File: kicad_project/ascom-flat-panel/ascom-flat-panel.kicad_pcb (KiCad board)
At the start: 4 copper layers, 55 x 29.5 mm, 14 parts, among them J1 Servo, J2 JST-XH LED, Q1 IRLZ34N, Q2 IRLZ34N, U1 XIAO-SAMD21-DIP

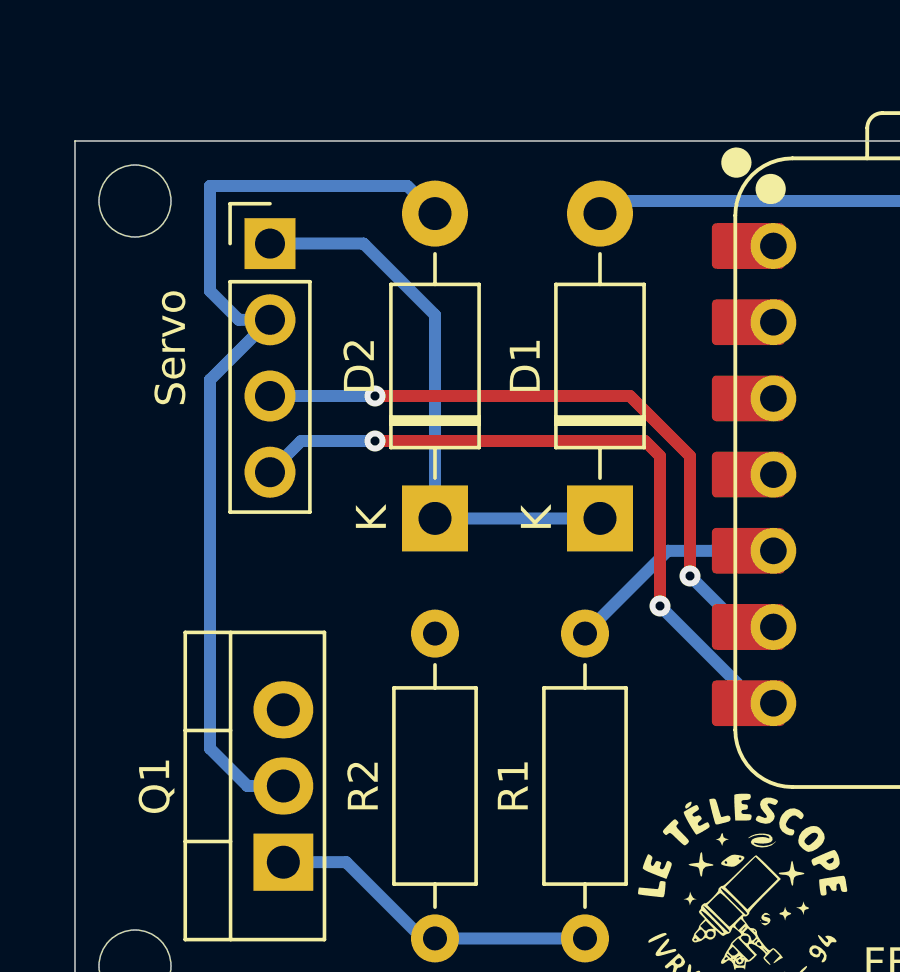
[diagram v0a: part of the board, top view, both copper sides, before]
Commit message: [kicad] - Modif suite aux tests servo : valeur R2 + routage connecteur
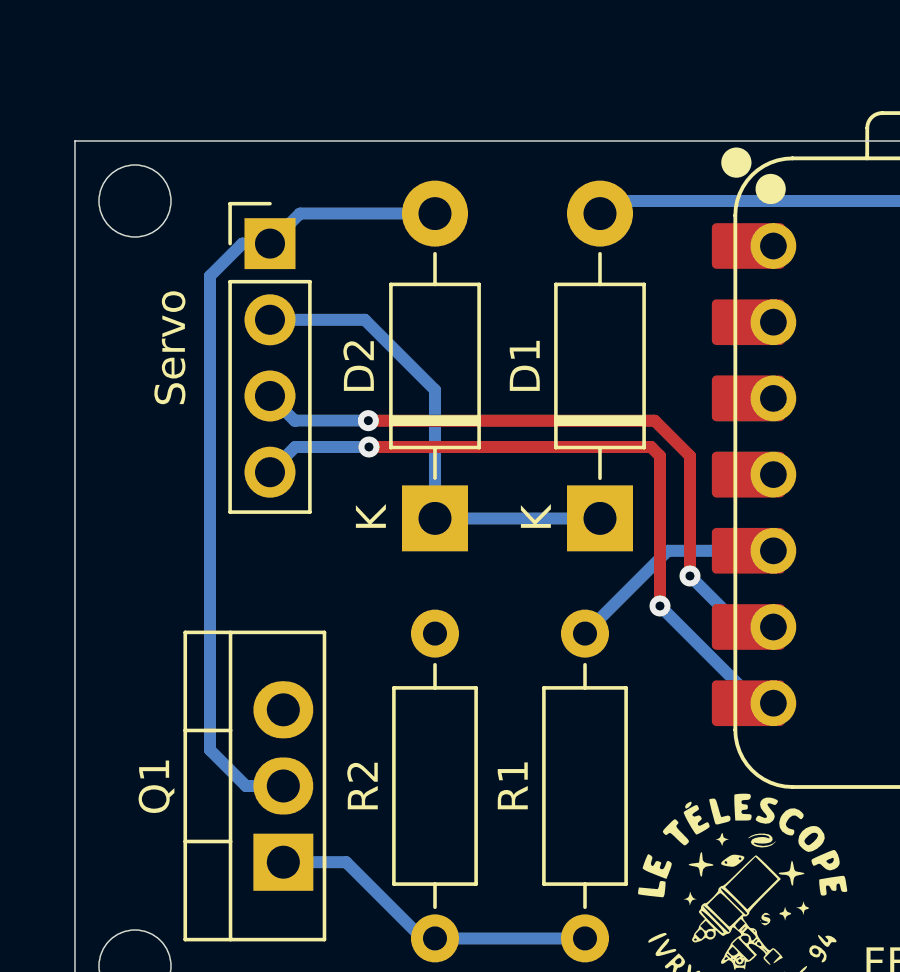
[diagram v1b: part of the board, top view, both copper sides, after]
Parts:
- R2: value 2kΩ -> 2.2kΩ
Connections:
- J1 pad 1: SERVO VCC -> SERVO GND
- J1 pad 2: SERVO GND -> SERVO VCC
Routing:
- net SERVO GND: track 31.9 -> 27.1 mm
- net SERVO VCC: track 18.8 -> 16.2 mm
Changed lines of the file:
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@@
 			)
 		)
-		(property "Value" "2kΩ"
+		(property "Value" "2.2kΩ"
 			(at 5.08 2.37 90)
 			(layer "F.Fab")
@@
 			(layers "*.Cu" "*.Mask")
 			(remove_unused_layers no)
-			(net 3 "SERVO VCC")
+			(net 4 "SERVO GND")
 			(pinfunction "Pin_1")
 			(pintype "passive")
@@
 			(layers "*.Cu" "*.Mask")
 			(remove_unused_layers no)
-			(net 4 "SERVO GND")
+			(net 3 "SERVO VCC")
 			(pinfunction "Pin_2")
 			(pintype "passive")
@@
 	)
 	(segment
-		(start 106.62 72.92)
-		(end 103.5 72.92)
+		(start 114.5 82.08)
+		(end 109 82.08)
 		(width 0.4)
 		(layer "B.Cu")
@@
 	)
 	(segment
-		(start 114.5 82.08)
-		(end 109 82.08)
+		(start 109 82.08)
+		(end 109 77.8)
 		(width 0.4)
 		(layer "B.Cu")
@@
 	)
 	(segment
-		(start 109 75.3)
-		(end 106.62 72.92)
+		(start 109 77.8)
+		(end 106.66 75.46)
 		(width 0.4)
 		(layer "B.Cu")
@@
 	)
 	(segment
-		(start 109 82.08)
-		(end 109 75.3)
+		(start 106.66 75.46)
+		(end 103.5 75.46)
 		(width 0.4)
 		(layer "B.Cu")
@@
 	)
 	(segment
-		(start 109 71.92)
-		(end 108.08 71)
+		(start 103.945 91)
+		(end 102.7 91)
 		(width 0.4)
 		(layer "B.Cu")
@@
 	)
 	(segment
-		(start 102.75 91)
-		(end 101.5 89.75)
+		(start 102.58 72.92)
+		(end 103.5 72.92)
 		(width 0.4)
 		(layer "B.Cu")
@@
 	)
 	(segment
-		(start 101.5 77.46)
-		(end 103.5 75.46)
+		(start 102.7 91)
+		(end 101.5 89.8)
 		(width 0.4)
 		(layer "B.Cu")
@@
 	)
 	(segment
-		(start 108.08 71)
-		(end 101.5 71)
+		(start 101.5 74)
+		(end 102.58 72.92)
 		(width 0.4)
 		(layer "B.Cu")
@@
 	)
 	(segment
-		(start 102.46 75.46)
-		(end 103.5 75.46)
+		(start 101.5 89.8)
+		(end 101.5 74)
 		(width 0.4)
 		(layer "B.Cu")
@@
 	)
 	(segment
-		(start 101.5 89.75)
-		(end 101.5 77.46)
+		(start 104.5 71.92)
+		(end 103.5 72.92)
 		(width 0.4)
 		(layer "B.Cu")
@@
 	)
 	(segment
-		(start 103.945 91)
-		(end 102.75 91)
+		(start 109 71.92)
+		(end 104.5 71.92)
 		(width 0.4)
 		(layer "B.Cu")
@@
 	)
 	(segment
-		(start 101.5 74.5)
-		(end 102.46 75.46)
-		(width 0.4)
-		(layer "B.Cu")
-		(net 4)
-	)
-	(segment
-		(start 101.5 71)
-		(end 101.5 74.5)
-		(width 0.4)
-		(layer "B.Cu")
-		(net 4)
-	)
-	(segment
-		(start 116 79.5)
-		(end 107 79.5)
+		(start 116.5 80)
+		(end 116.5 85)
 		(width 0.4)
 		(layer "F.Cu")
@@
 	)
 	(segment
-		(start 116.5 85)
+		(start 116.2 79.7)
 		(end 116.5 80)
 		(width 0.4)
@@
 	)
 	(segment
-		(start 116.5 80)
-		(end 116 79.5)
+		(start 106.8 79.7)
+		(end 116.2 79.7)
 		(width 0.4)
 		(layer "F.Cu")
@@
 	)
 	(via
-		(at 107 79.5)
+		(at 106.8 79.7)
 		(size 0.7)
 		(drill 0.3)
@@
 	)
 	(segment
-		(start 104.54 79.5)
-		(end 103.5 80.54)
+		(start 106.8 79.7)
+		(end 104.34 79.7)
 		(width 0.4)
 		(layer "B.Cu")
@@
 	)
 	(segment
+		(start 104.34 79.7)
+		(end 103.5 80.54)
+		(width 0.4)
+		(layer "B.Cu")
+		(net 5)
+	)
+	(segment
 		(start 120.28 88.24)
 		(end 119.74 88.24)
@@
 	)
 	(segment
-		(start 107 79.5)
-		(end 104.54 79.5)
-		(width 0.4)
-		(layer "B.Cu")
-		(net 5)
-	)
-	(segment
-		(start 117.5 84)
-		(end 117.5 80)
+		(start 106.778 78.822)
+		(end 106.781 78.825)
 		(width 0.4)
 		(layer "F.Cu")
@@
 	)
 	(segment
-		(start 115.5 78)
-		(end 107 78)
+		(start 117.5 80)
+		(end 117.5 84)
 		(width 0.4)
 		(layer "F.Cu")
@@
 	)
 	(segment
-		(start 117.5 80)
-		(end 115.5 78)
+		(start 116.325 78.825)
+		(end 117.5 80)
 		(width 0.4)
 		(layer "F.Cu")
 		(net 6)
 	)
+	(segment
+		(start 106.781 78.825)
+		(end 116.325 78.825)
+		(width 0.4)
+		(layer "F.Cu")
+		(net 6)
+	)
 	(via
-		(at 107 78)
+		(at 106.778 78.822)
 		(size 0.7)
 		(drill 0.3)
@@
 	)
 	(segment
+		(start 106.778 78.822)
+		(end 104.322 78.822)
+		(width 0.4)
+		(layer "B.Cu")
+		(net 6)
+	)
+	(segment
 		(start 119.2 85.7)
 		(end 117.5 84)
@@
 	)
 	(segment
-		(start 107 78)
+		(start 104.322 78.822)
 		(end 103.5 78)
 		(width 0.4)

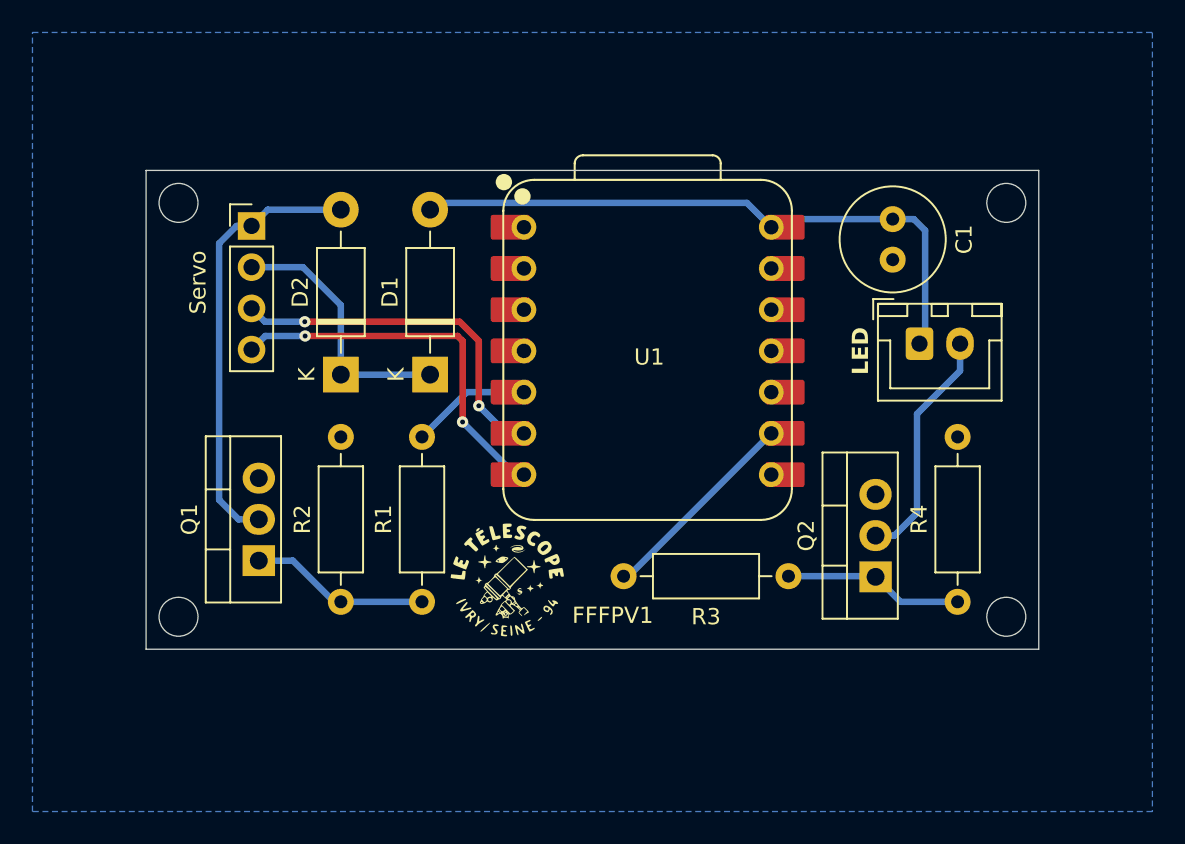
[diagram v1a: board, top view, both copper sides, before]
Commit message: [kicad] - optimisation placement des connecteurs
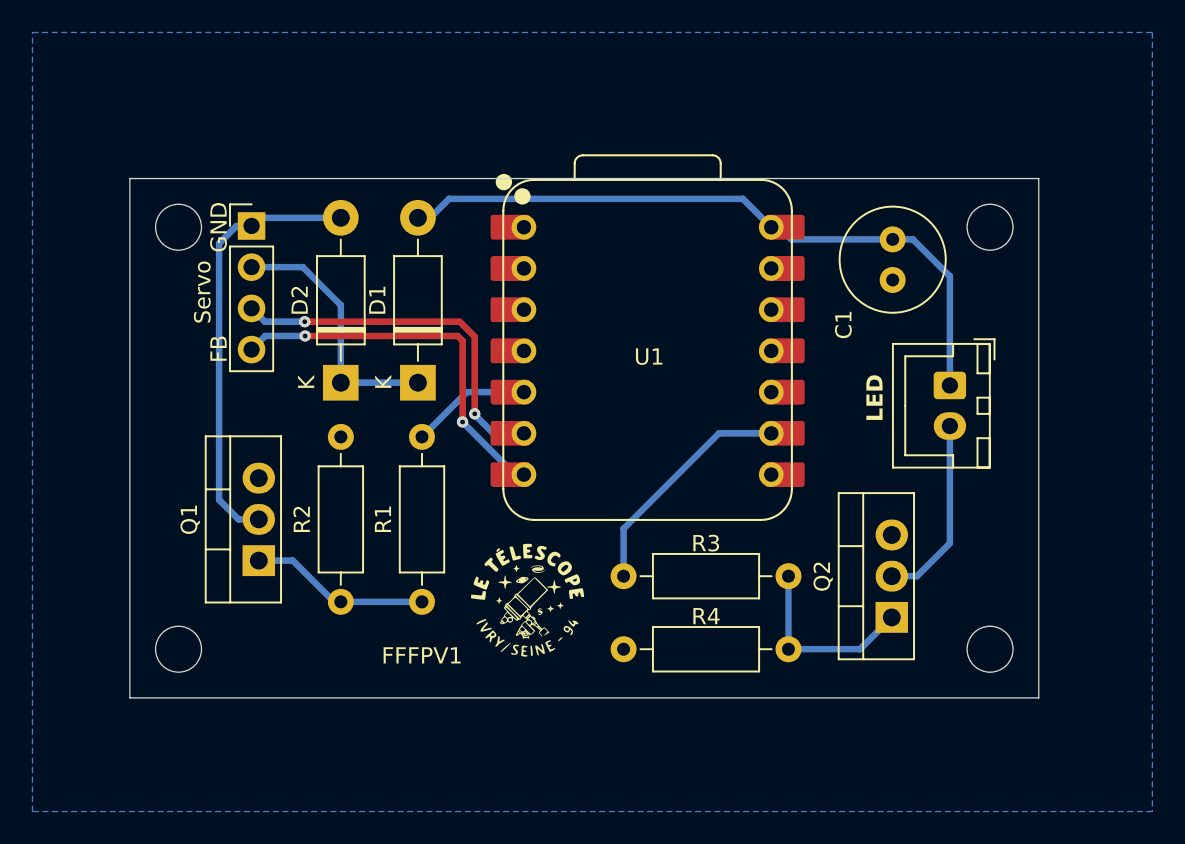
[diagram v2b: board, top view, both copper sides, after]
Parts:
- moved R4 10.8 mm to (136.6, 99.0), turned to 180 degrees
- moved J2 3.19 mm to (146.5, 82.8), turned to -90 degrees
- moved Q2 2.69 mm to (142.9, 97.0)
- moved G*** 1.77 mm to (120.5, 96.0)
- moved C1 1.25 mm to (143.0, 73.8)
- moved D1 0.90 mm to (113.8, 82.6)
- moved D2 0.50 mm to (109.0, 82.6)
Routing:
- net Net-(J2-Pin_2): track 14.7 -> 11.6 mm
- net +5V: track 38.9 -> 41.2 mm
- net LED_STRIP_POWER_CONTROL: track 12.7 -> 14.5 mm
- net Net-(Q2-G): track 13.1 -> 11.7 mm
- net SERVO VCC: track 16.2 -> 15.5 mm
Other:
- board size 55 x 29.5 mm -> 56 x 32 mm
- board text added: "FB"
- board text added: "GND"

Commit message: [kicad] - suppression des vias, ajustement des trous (M2) et arrondi des angles
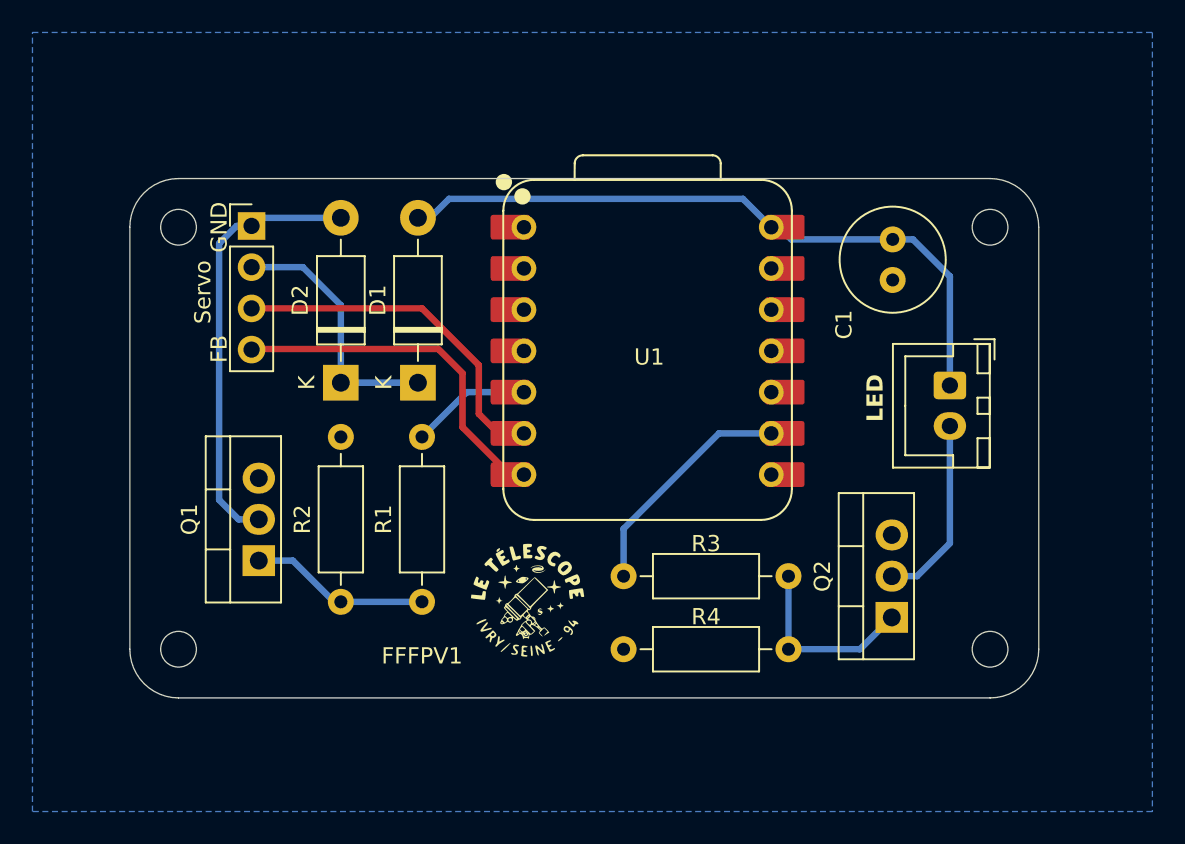
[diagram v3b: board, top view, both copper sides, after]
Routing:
- net SERVO POSITION FEEDBACK: track 23.6 -> 22.5 mm, vias 2 -> 0
- net SERVO POSITION CONTROL: track 22.8 -> 21.7 mm, vias 2 -> 0
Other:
- outline, holes or cut-outs redrawn
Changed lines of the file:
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@@
 	(gr_circle
 		(center 99 99)
-		(end 100 98)
+		(end 100.1 99)
 		(stroke
 			(width 0.05)
@@
 		(layer "Edge.Cuts")
 	)
+	(gr_arc
+		(start 152 99)
+		(mid 151.12132 101.12132)
+		(end 149 102)
+		(stroke
+			(width 0.05)
+			(type default)
+		)
+		(layer "Edge.Cuts")
+	)
 	(gr_line
-		(start 96 102)
-		(end 152 102)
+		(start 99 102)
+		(end 149 102)
 		(stroke
 			(width 0.05)
@@
 	(gr_circle
 		(center 99 73)
-		(end 100 72)
+		(end 100.1 73)
 		(stroke
 			(width 0.05)
@@
 	(gr_circle
 		(center 149 99)
-		(end 150 98)
+		(end 150.1 99)
 		(stroke
 			(width 0.05)
@@
 		(layer "Edge.Cuts")
 	)
+	(gr_arc
+		(start 99 102)
+		(mid 96.87868 101.12132)
+		(end 96 99)
+		(stroke
+			(width 0.05)
+			(type default)
+		)
+		(layer "Edge.Cuts")
+	)
 	(gr_line
-		(start 152 70)
-		(end 152 102)
+		(start 152 73)
+		(end 152 99)
 		(stroke
 			(width 0.05)
@@
 	)
 	(gr_line
-		(start 96 70)
-		(end 96 102)
+		(start 96 73)
+		(end 96 99)
+		(stroke
+			(width 0.05)
+			(type default)
+		)
+		(layer "Edge.Cuts")
+	)
+	(gr_arc
+		(start 149 70)
+		(mid 151.12132 70.87868)
+		(end 152 73)
 		(stroke
 			(width 0.05)
@@
 	(gr_circle
 		(center 149 73)
-		(end 150 72)
+		(end 150.1 73)
 		(stroke
 			(width 0.05)
@@
 	)
 	(gr_line
-		(start 152 70)
-		(end 96 70)
+		(start 149 70)
+		(end 99 70)
+		(stroke
+			(width 0.05)
+			(type default)
+		)
+		(layer "Edge.Cuts")
+	)
+	(gr_arc
+		(start 96 73)
+		(mid 96.87868 70.87868)
+		(end 99 70)
 		(stroke
 			(width 0.05)
@@
 	)
 	(segment
-		(start 116.5 80)
-		(end 116.5 85)
-		(width 0.4)
-		(layer "F.Cu")
-		(net 5)
-	)
-	(segment
-		(start 116.2 79.7)
-		(end 116.5 80)
-		(width 0.4)
-		(layer "F.Cu")
-		(net 5)
-	)
-	(segment
-		(start 106.8 79.7)
-		(end 116.2 79.7)
-		(width 0.4)
-		(layer "F.Cu")
-		(net 5)
-	)
-	(via
-		(at 116.5 85)
-		(size 0.7)
-		(drill 0.3)
-		(layers "F.Cu" "B.Cu")
-		(net 5)
-	)
-	(via
-		(at 106.8 79.7)
-		(size 0.7)
-		(drill 0.3)
-		(layers "F.Cu" "B.Cu")
-		(net 5)
-	)
-	(segment
-		(start 119.74 88.24)
-		(end 116.5 85)
-		(width 0.4)
-		(layer "B.Cu")
-		(net 5)
-	)
-	(segment
-		(start 106.8 79.7)
-		(end 104.34 79.7)
-		(width 0.4)
-		(layer "B.Cu")
-		(net 5)
-	)
-	(segment
-		(start 104.34 79.7)
+		(start 103.54 80.5)
 		(end 103.5 80.54)
 		(width 0.4)
-		(layer "B.Cu")
+		(layer "F.Cu")
+		(net 5)
+	)
+	(segment
+		(start 116.5 85.33)
+		(end 116.5 82)
+		(width 0.4)
+		(layer "F.Cu")
+		(net 5)
+	)
+	(segment
+		(start 115 80.5)
+		(end 103.54 80.5)
+		(width 0.4)
+		(layer "F.Cu")
+		(net 5)
+	)
+	(segment
+		(start 116.5 82)
+		(end 115 80.5)
+		(width 0.4)
+		(layer "F.Cu")
+		(net 5)
+	)
+	(segment
+		(start 119.41 88.24)
+		(end 116.5 85.33)
+		(width 0.4)
+		(layer "F.Cu")
+		(net 5)
+	)
+	(segment
+		(start 120.28 88.24)
+		(end 119.41 88.24)
+		(width 0.4)
+		(layer "F.Cu")
 		(net 5)
 	)
@@
 	)
 	(segment
-		(start 116.325 78.825)
-		(end 106.781 78.825)
-		(width 0.4)
-		(layer "F.Cu")
-		(net 6)
-	)
-	(segment
-		(start 106.781 78.825)
-		(end 106.778 78.822)
-		(width 0.4)
-		(layer "F.Cu")
-		(net 6)
-	)
-	(segment
-		(start 117.25 84.5)
-		(end 117.25 79.75)
-		(width 0.4)
-		(layer "F.Cu")
-		(net 6)
-	)
-	(segment
-		(start 117.25 79.75)
-		(end 116.325 78.825)
-		(width 0.4)
-		(layer "F.Cu")
-		(net 6)
-	)
-	(via
-		(at 106.778 78.822)
-		(size 0.7)
-		(drill 0.3)
-		(layers "F.Cu" "B.Cu")
-		(net 6)
-	)
-	(via
-		(at 117.25 84.5)
-		(size 0.7)
-		(drill 0.3)
-		(layers "F.Cu" "B.Cu")
-		(net 6)
-	)
-	(segment
-		(start 106.778 78.822)
-		(end 104.322 78.822)
-		(width 0.4)
-		(layer "B.Cu")
-		(net 6)
-	)
-	(segment
-		(start 117.25 84.5)
-		(end 117.25 84.55)
-		(width 0.4)
-		(layer "B.Cu")
-		(net 6)
-	)
-	(segment
-		(start 117.25 84.55)
-		(end 118.4 85.7)
-		(width 0.4)
-		(layer "B.Cu")
-		(net 6)
-	)
-	(segment
-		(start 118.4 85.7)
-		(end 120.28 85.7)
-		(width 0.4)
-		(layer "B.Cu")
-		(net 6)
-	)
-	(segment
-		(start 104.322 78.822)
+		(start 120.28 85.7)
+		(end 118.7 85.7)
+		(width 0.4)
+		(layer "F.Cu")
+		(net 6)
+	)
+	(segment
+		(start 114 78)
 		(end 103.5 78)
 		(width 0.4)
-		(layer "B.Cu")
-		(net 6)
-	)
+		(layer "F.Cu")
+		(net 6)
+	)
+	(segment
+		(start 117.5 81.5)
+		(end 114 78)
+		(width 0.4)
+		(layer "F.Cu")
+		(net 6)
+	)
+	(segment
+		(start 117.5 84.5)
+		(end 117.5 81.5)
+		(width 0.4)
+		(layer "F.Cu")
+		(net 6)
+	)
+	(segment
+		(start 118.7 85.7)
+		(end 117.5 84.5)
+		(width 0.4)
+		(layer "F.Cu")
+		(net 6)
+	)

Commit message: [kicad] - suppression des 2 couches internes de Cu inutiles suite à reviex pcbway. Mise à jour du pcb et des fichiers gerber (#14)
* [kicad] - génération des fichiers pour la commande !!

* [kicad] - suppression des 2 couches internes de Cu inutiles suite à reviex pcbway. Mise à jour du pcb et des fichiers gerber

---------

Co-authored-by: ft7588 <flthibaud@gmail.com>
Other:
- copper layers 4 -> 2
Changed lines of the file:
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@@
 	(layers
 		(0 "F.Cu" signal)
-		(4 "In1.Cu" signal)
-		(6 "In2.Cu" signal)
 		(2 "B.Cu" signal)
 		(13 "F.Paste" user)
@@
 			(layer "dielectric 1"
 				(type "core")
-				(thickness 0.480066)
-				(material "FR4")
-				(epsilon_r 4.5)
-				(loss_tangent 0.02)
-			)
-			(layer "In1.Cu"
-				(type "copper")
-				(thickness 0.035)
-			)
-			(layer "dielectric 2"
-				(type "prepreg")
-				(thickness 0.480066)
-				(material "FR4")
-				(epsilon_r 4.5)
-				(loss_tangent 0.02)
-			)
-			(layer "In2.Cu"
-				(type "copper")
-				(thickness 0.035)
-			)
-			(layer "dielectric 3"
-				(type "core")
-				(thickness 0.480066)
+				(thickness 1.510198)
 				(material "FR4")
 				(epsilon_r 4.5)
@@
 		)
 		(pad_to_mask_clearance 0)
-		(solder_mask_min_width 0.1016)
 		(allow_soldermask_bridges_in_footprints no)
 		(tenting front back)
